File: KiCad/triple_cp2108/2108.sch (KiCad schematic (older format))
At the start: 75 parts, among them IC1 CP2108-B03-GMR, J19 Screw_Terminal_01x09, J20 Screw_Terminal_01x09, J21 Screw_Terminal_01x09, J22 Screw_Terminal_01x09, J23 RJ12, J24 RJ12, J25 RJ12, J26 RJ12, U11 SP3243, U12 SP3243, U13 SP3243, U14 SP3243

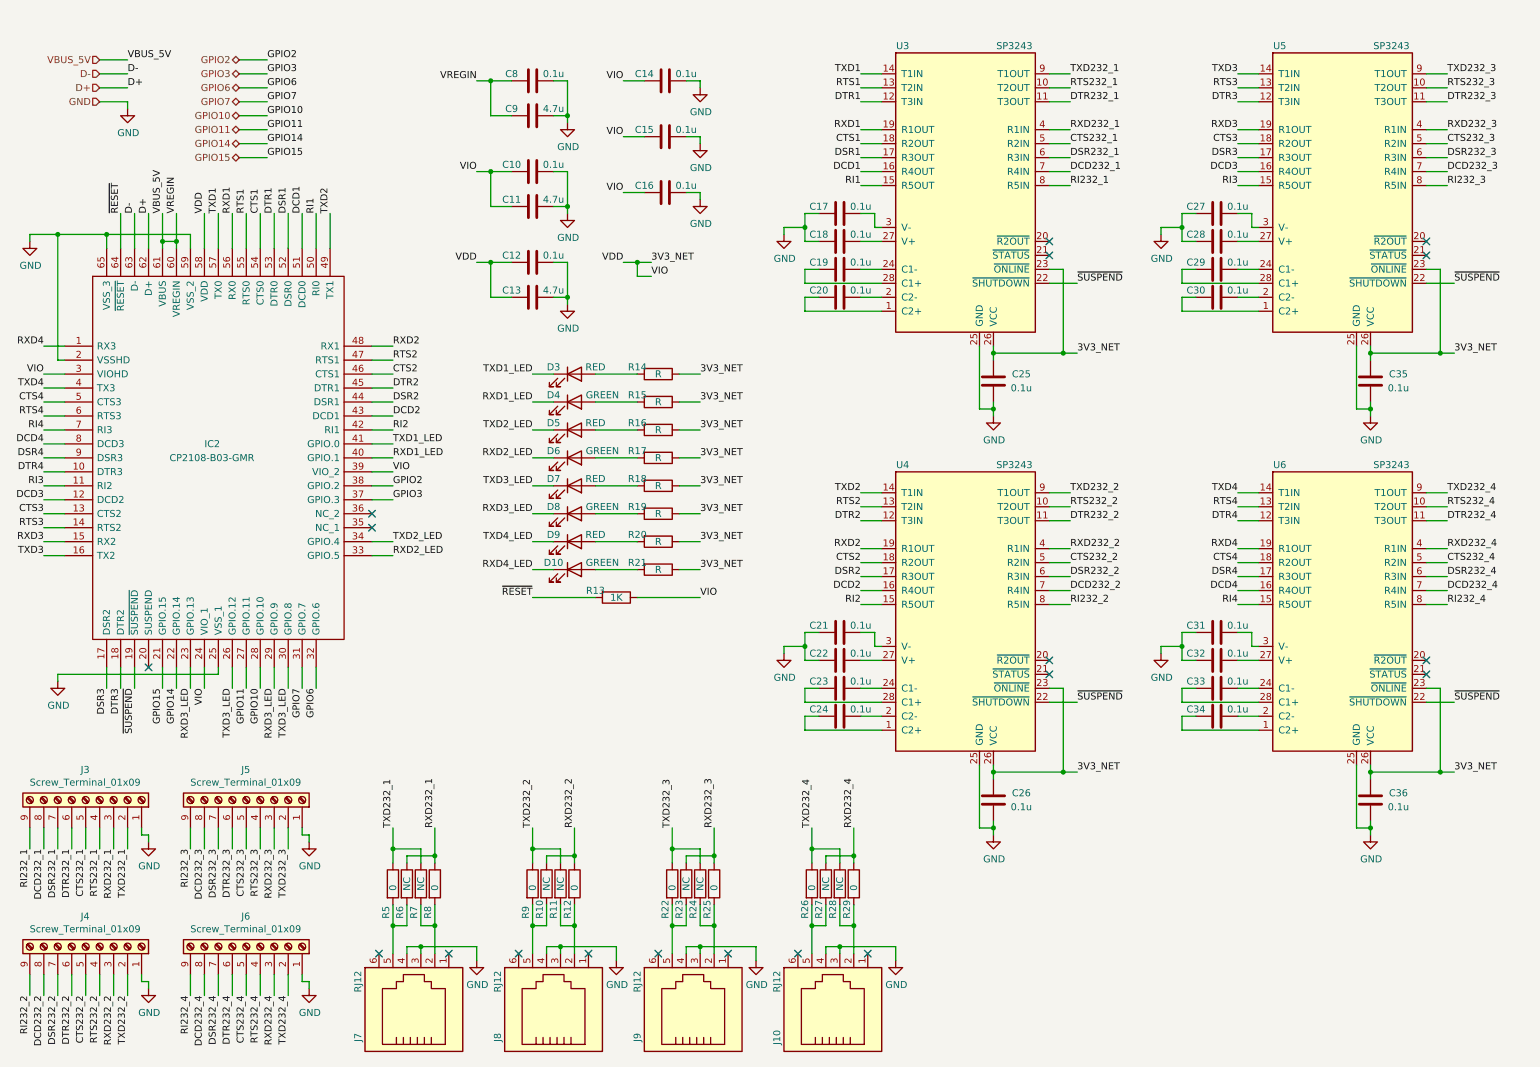
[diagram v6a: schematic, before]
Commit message: Diodes changed
USB ESD protection diodes changed to individual ones
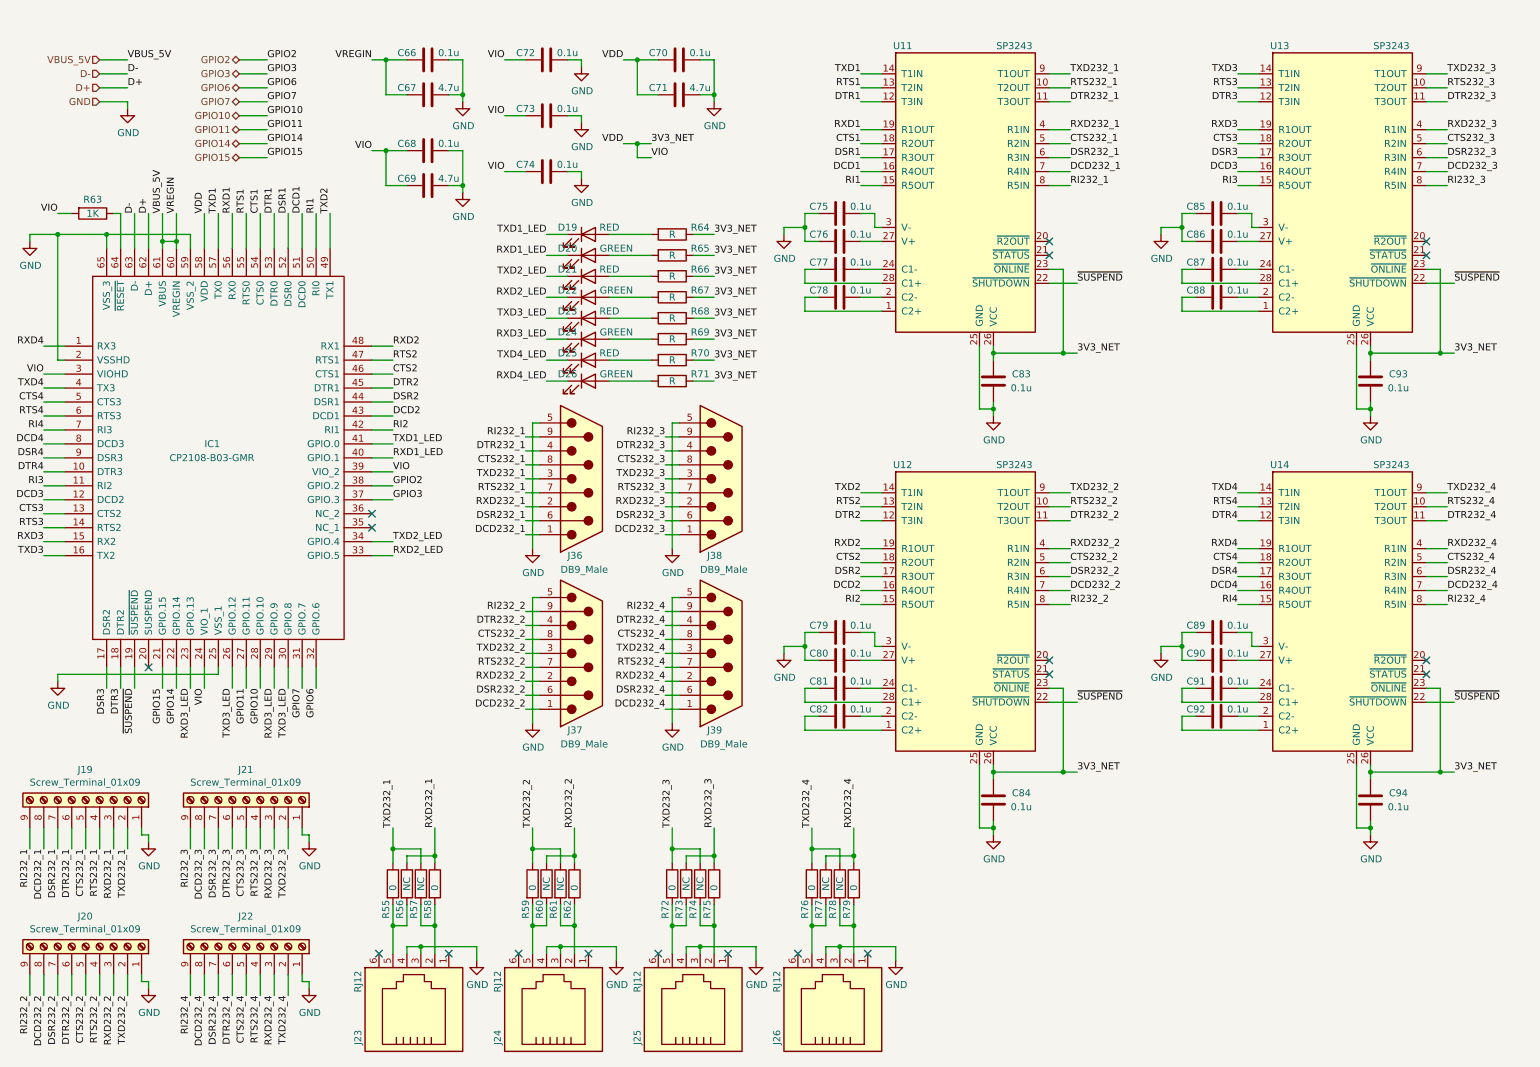
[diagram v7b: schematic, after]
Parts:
- added J28, J29, J30, J31: DB9_Male, Connector_Dsub:DSUB-9_Male_EdgeMount_P2.77mm, symbol Connector:DB9_Male
- C66, C67, C68, C69, C70, C71, C72, C73, C74, C75, C76, C77, C78, C79, C80, C81, C82, C83, C84, C85, C86, C87, C88, C89, C90, C91, C92, C93, C94: footprint (none) -> Capacitor_SMD:C_2225_5664Metric
- D19, D20, D21, D22, D23, D24, D25, D26: footprint (none) -> LED_SMD:LED_1206_3216Metric
- IC1: footprint QFN50P900X900X90-65N-D -> Samacsys:QFN50P900X900X90-65N-D
- J19, J20, J21, J22: footprint (none) -> Connector_PinHeader_1.00mm:PinHeader_1x09_P1.00mm_Horizontal
- R55, R56, R57, R58, R59, R60, R61, R62, R63, R64, R65, R66, R67, R68, R69, R70, R71, R72, R73, R74, R75, R76, R77, R78, R79: footprint (none) -> Resistor_SMD:R_1206_3216Metric
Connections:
- net 3V3_NET: now also R63.2; no longer R63.1
- net CTS232_1: now also J28.8
- net CTS232_2: now also J29.8
- net CTS232_3: now also J30.8
- net CTS232_4: now also J31.8
- net DCD232_1: now also J28.1
- net DCD232_2: now also J29.1
- net DCD232_3: now also J30.1
- net DCD232_4: now also J31.1
- net DSR232_1: now also J28.6
- net DSR232_2: now also J29.6
- net DSR232_3: now also J30.6
- net DSR232_4: now also J31.6
- net DTR232_1: now also J28.4
- net DTR232_2: now also J29.4
- net DTR232_3: now also J30.4
- net DTR232_4: now also J31.4
- net GND: now also J28.5, J29.5, J30.5, J31.5
- net RI232_1: now also J28.9
- net RI232_2: now also J29.9
- net RI232_3: now also J30.9
- net RI232_4: now also J31.9
- net RTS232_1: now also J28.7
- net RTS232_2: now also J29.7
- net RTS232_3: now also J30.7
- net RTS232_4: now also J31.7
- net RXD232_1: now also J28.2
- net RXD232_2: now also J29.2
- net RXD232_3: now also J30.2
- net RXD232_4: now also J31.2
- net TXD232_1: now also J28.3
- net TXD232_2: now also J29.3
- net TXD232_3: now also J30.3
- net TXD232_4: now also J31.3
- net ~RESET: no longer names the net of IC1.64 (~RESET)
- net ~RESET: now also R63.1; no longer R63.2
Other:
- moved on the sheet: C66, C67, C68, C69, C70, C71, C72, C73, C74, D19, D20, D21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

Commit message: BOM consolidation 1
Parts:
- C66, C68, C70, C72, C73, C74, C75, C76, C77, C78, C79, C80, C81, C82, C83, C84, C85, C86, C87, C88, C89, C90, C91, C92, C93, C94: footprint Capacitor_SMD:C_2225_5664Metric -> Capacitor_SMD:C_0805_2012Metric_Pad1.18x1.45mm_HandSolder; Manufacturer_Part_Number (none) -> C0805C104M5RACTU; Mouser Price/Stock (none) -> https://www.eleparts.co.kr/goods/view?no=8550995
- C67, C69, C71: footprint Capacitor_SMD:C_2225_5664Metric -> (none)
- D19, D21, D23, D25: footprint LED_SMD:LED_1206_3216Metric -> LED_SMD:LED_0603_1608Metric; Description (none) -> LTST-C193KRKT-5A; Manufacturer_Name (none) -> Lite-On; Manufacturer_Part_Number (none) -> LTST-C193KRKT-5A; Mouser Price/Stock (none) -> https://www.eleparts.co.kr/goods/view?no=7578730
- D20, D22, D24, D26: footprint LED_SMD:LED_1206_3216Metric -> LED_SMD:LED_0603_1608Metric; Description (none) -> LTST-C193KGKT-5A; Manufacturer_Name (none) -> Lite-On; Manufacturer_Part_Number (none) -> LTST-C193KGKT-5A; Mouser Price/Stock (none) -> https://www.eleparts.co.kr/goods/view?no=7578641
